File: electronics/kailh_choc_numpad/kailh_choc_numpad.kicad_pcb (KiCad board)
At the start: 2 copper layers, 100 x 88 mm, 134 parts, among them J1 Conn_01x06, U1 PCA9554, U2 PCA9535

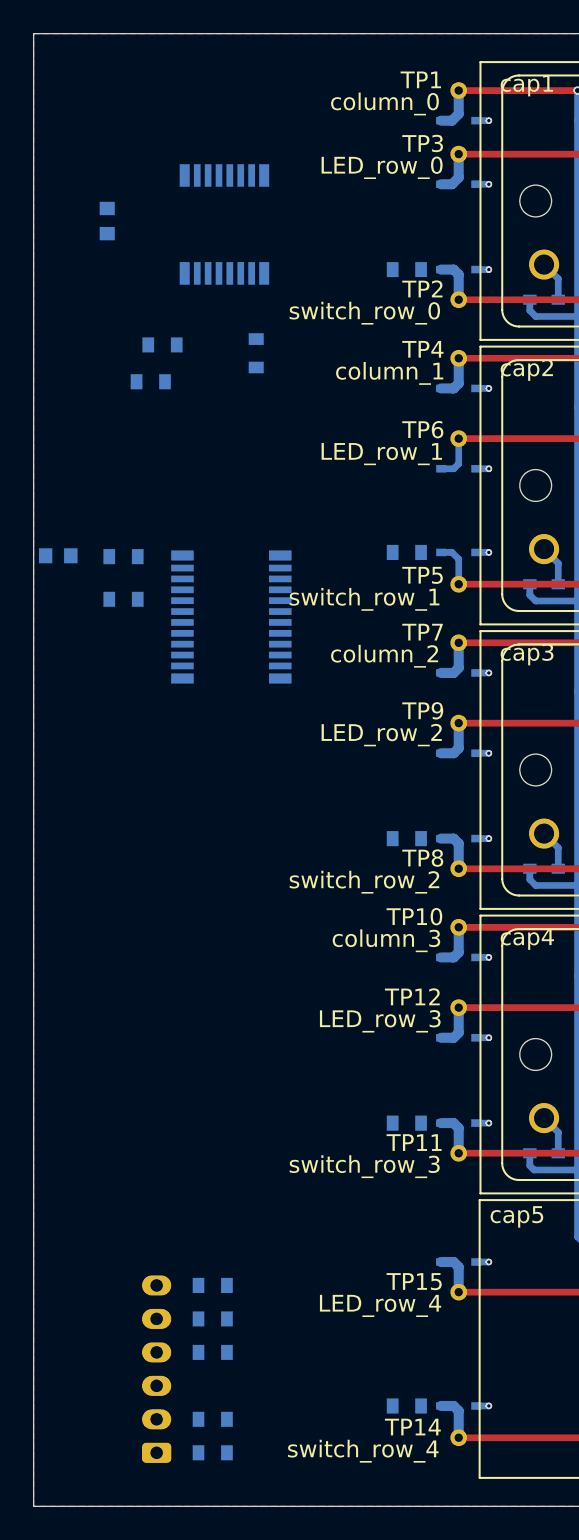
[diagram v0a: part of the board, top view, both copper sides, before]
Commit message: further placing and routing
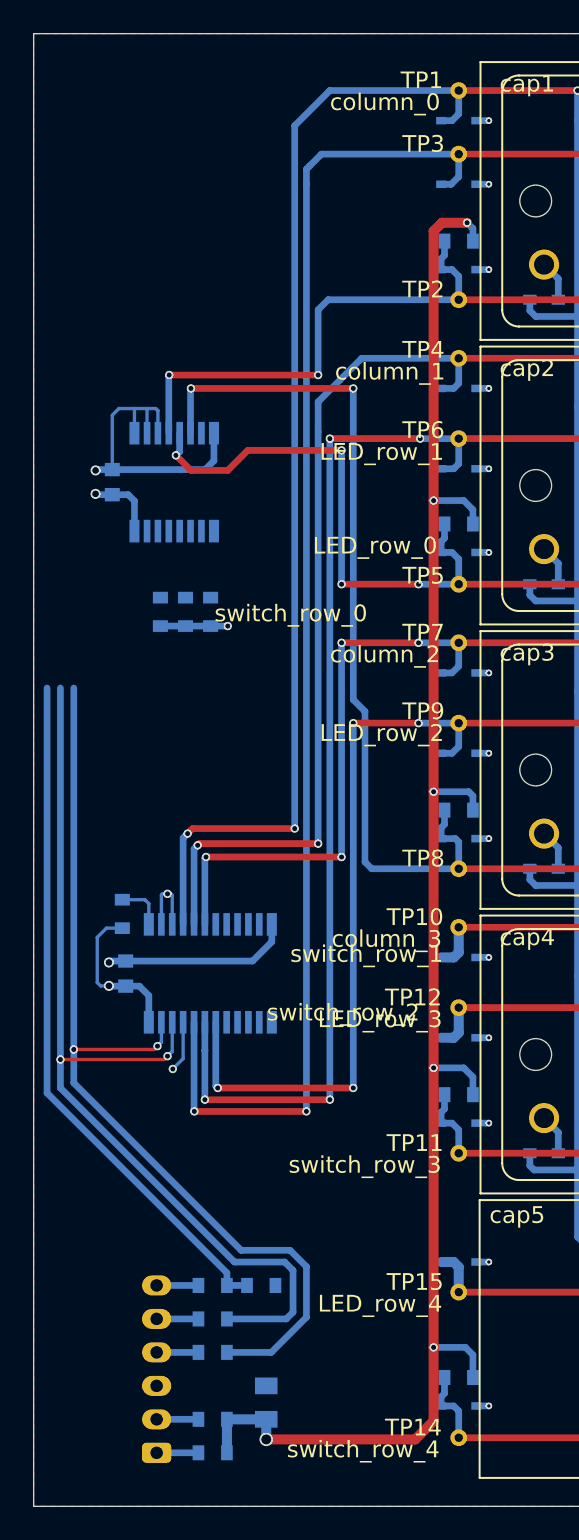
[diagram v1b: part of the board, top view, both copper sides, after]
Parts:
- added C3: 10u, SquantorRcl:C_0805, B.Cu at (148.4, 151.8)
- moved R32 41.8 mm to (148.1, 144.8), turned to 0 degrees
- moved C2 25.3 mm to (140.0, 126.2), turned to -90 degrees
- moved R31 21.4 mm to (139.8, 122.6), turned to 90 degrees
- moved U2 21.3 mm to (145.1, 126.2), turned to -90 degrees
- moved R29 16.0 mm to (143.6, 104.5)
- moved R30 16.0 mm to (142.1, 104.5), turned to 90 degrees
- moved U1 15.7 mm to (142.9, 96.8)
- moved C1 15.6 mm to (139.2, 96.8)
- moved R28 14.2 mm to (145.1, 104.5), turned to 90 degrees
- moved R24 3.54 mm to (159.9, 99.3), turned to 180 degrees
- moved R23 3.54 mm to (159.9, 82.4), turned to 180 degrees
- moved R25 3.54 mm to (159.9, 116.4), turned to 180 degrees
- moved R26 3.54 mm to (159.9, 133.4), turned to 180 degrees
- moved R27 3.54 mm to (159.9, 150.3), turned to 180 degrees
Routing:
- net VDD: track 0.00 -> 122.6 mm, vias 0 -> 9
- net /LED_row_0: track 72.8 -> 150.6 mm, vias 0 -> 2
- net /column_0: track 128.6 -> 193.3 mm, vias 1 -> 3
- net /LED_row_1: track 77.4 -> 136.7 mm, vias 0 -> 4
- net /SCL: track 0.00 -> 57.6 mm, vias 0 -> 2
- net /SDA: track 0.00 -> 57.3 mm, vias 0 -> 2
- net /switch_row_2: track 48.8 -> 97.4 mm, vias 0 -> 2
- net /column_1: track 113.2 -> 161.1 mm, vias 1 -> 3
- net /!INT: track 0.00 -> 41.4 mm
- net /LED_row_2: track 53.0 -> 93.1 mm, vias 0 -> 4
- net VSS: track 10.5 -> 48.5 mm, vias 14 -> 18
- net /column_2: track 154.2 -> 186.1 mm, vias 1 -> 5
- net /switch_row_1: track 73.1 -> 102.1 mm, vias 0 -> 4
- net /switch_row_0: track 66.8 -> 93.4 mm, vias 0 -> 2
- net Net-(R31-Pad2): track 0.00 -> 2.92 mm
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
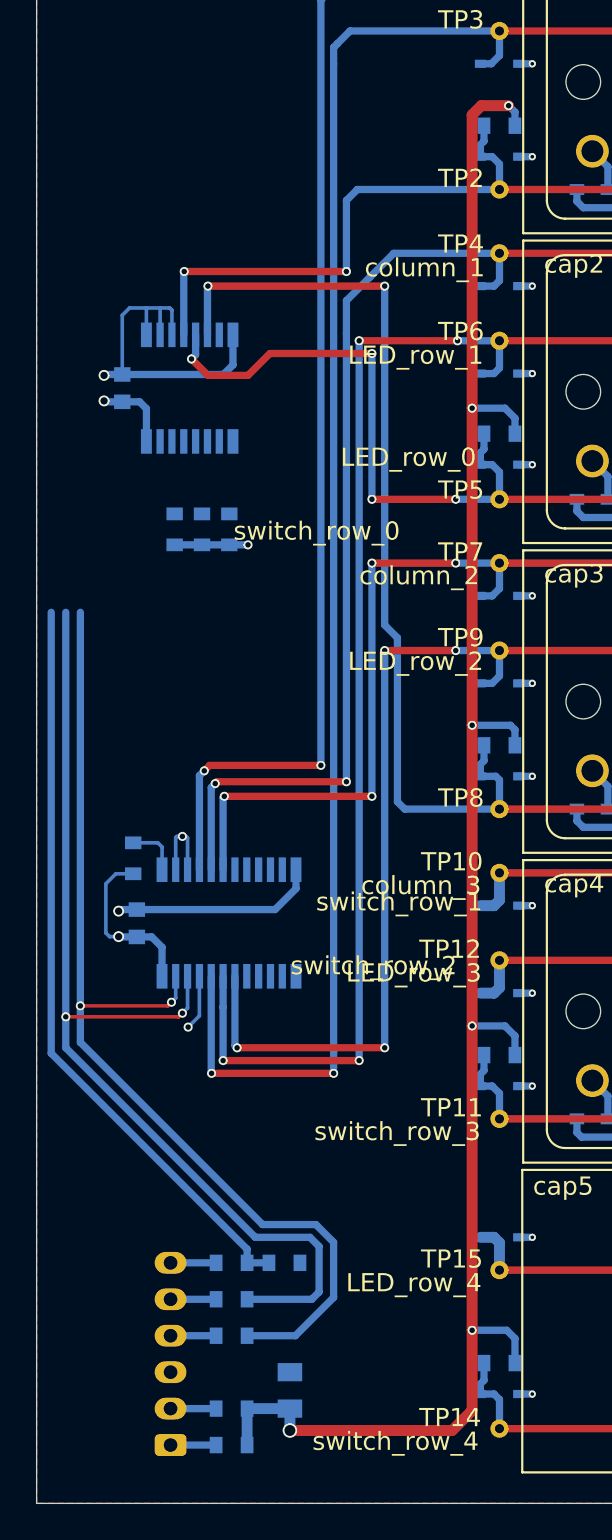
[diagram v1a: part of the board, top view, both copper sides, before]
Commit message: routed all traces
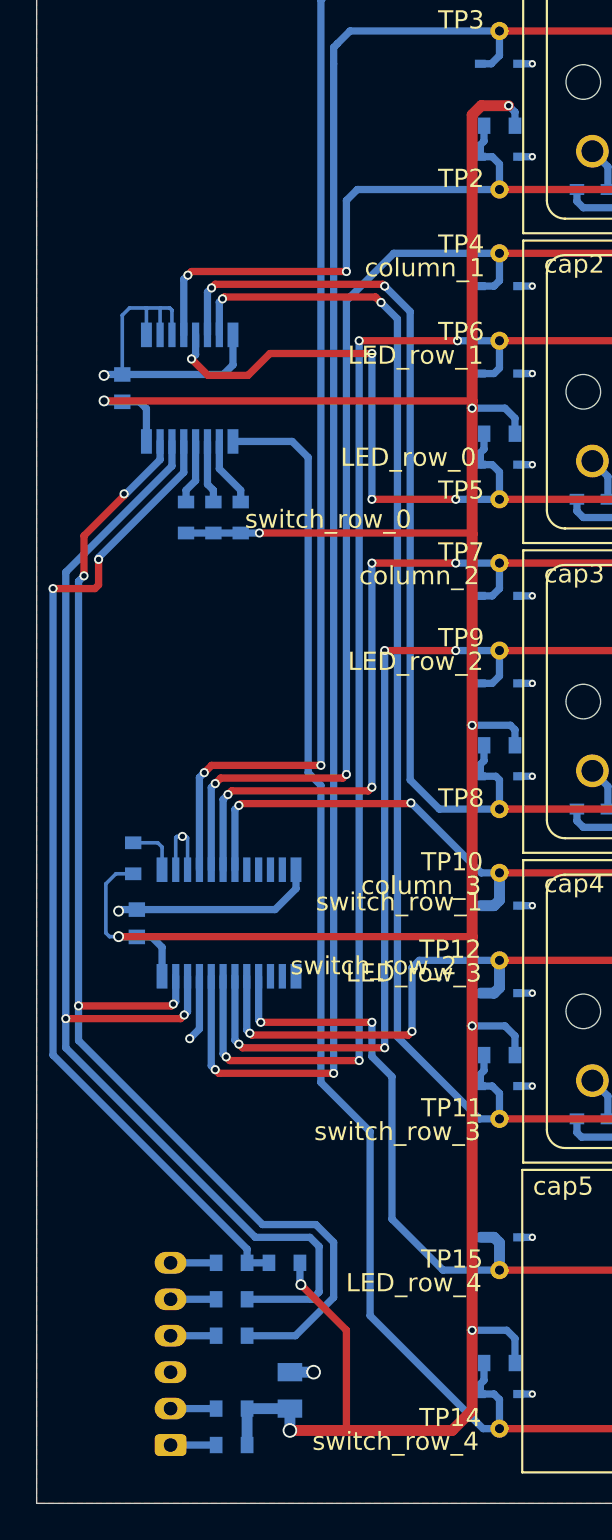
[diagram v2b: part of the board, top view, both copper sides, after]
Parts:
- moved R28 0.90 mm to (145.7, 103.9)
- moved R29 0.90 mm to (144.2, 103.9)
- moved R30 0.90 mm to (142.7, 103.9)
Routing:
- net /switch_row_4: track 50.7 -> 113.3 mm
- net VDD: track 122.6 -> 184.1 mm, vias 9 -> 10
- net /switch_row_3: track 74.6 -> 133.6 mm, vias 0 -> 2
- net /LED_row_4: track 51.0 -> 78.0 mm, vias 0 -> 2
- net /LED_row_3: track 77.4 -> 98.0 mm, vias 0 -> 2
- net /column_3: track 152.0 -> 171.6 mm, vias 1 -> 3
- net /!INT: track 41.4 -> 55.0 mm, vias 0 -> 2
- net /SCL: track 57.6 -> 69.5 mm
- net /SDA: track 57.3 -> 68.8 mm, vias 2 -> 4
- net /switch_row_5: track 0.00 -> 3.81 mm
- net /switch_row_7: track 0.00 -> 3.54 mm
- net /switch_row_6: track 0.00 -> 3.46 mm
- net VSS: track 48.5 -> 50.4 mm, vias 18 -> 19
- net /switch_row_2: track 97.4 -> 96.2 mm
